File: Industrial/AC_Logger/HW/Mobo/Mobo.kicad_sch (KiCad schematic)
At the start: 6 parts

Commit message: Started new PCB
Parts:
- added A1: Arduino_UNO_R3, For_Rasterboard:Arduino_UNO_R3_WithMountingHoles_Snapped_to_P2.54mm, symbol MCU_Module:Arduino_UNO_R3
- added RTC2: Conn_01x05_Female, Connector_PinSocket_2.54mm:PinSocket_1x05_P2.54mm_Vertical, symbol Connector:Conn_01x05_Female
- added microSD2: Conn_01x06_Female, Connector_PinSocket_2.00mm:PinSocket_1x06_P2.00mm_Vertical, symbol Connector:Conn_01x06_Female
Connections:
- new net +3V3: A1.4 (3V3), RTC2.1 (Pin_1), microSD2.1 (Pin_1)
- new net GND: A1.29 (GND), RTC2.2 (Pin_2)
- new net SCL: A1.32 (SCL/A5), RTC2.3 (Pin_3)
- new net SDA: A1.31 (SDA/A4), RTC2.4 (Pin_4)

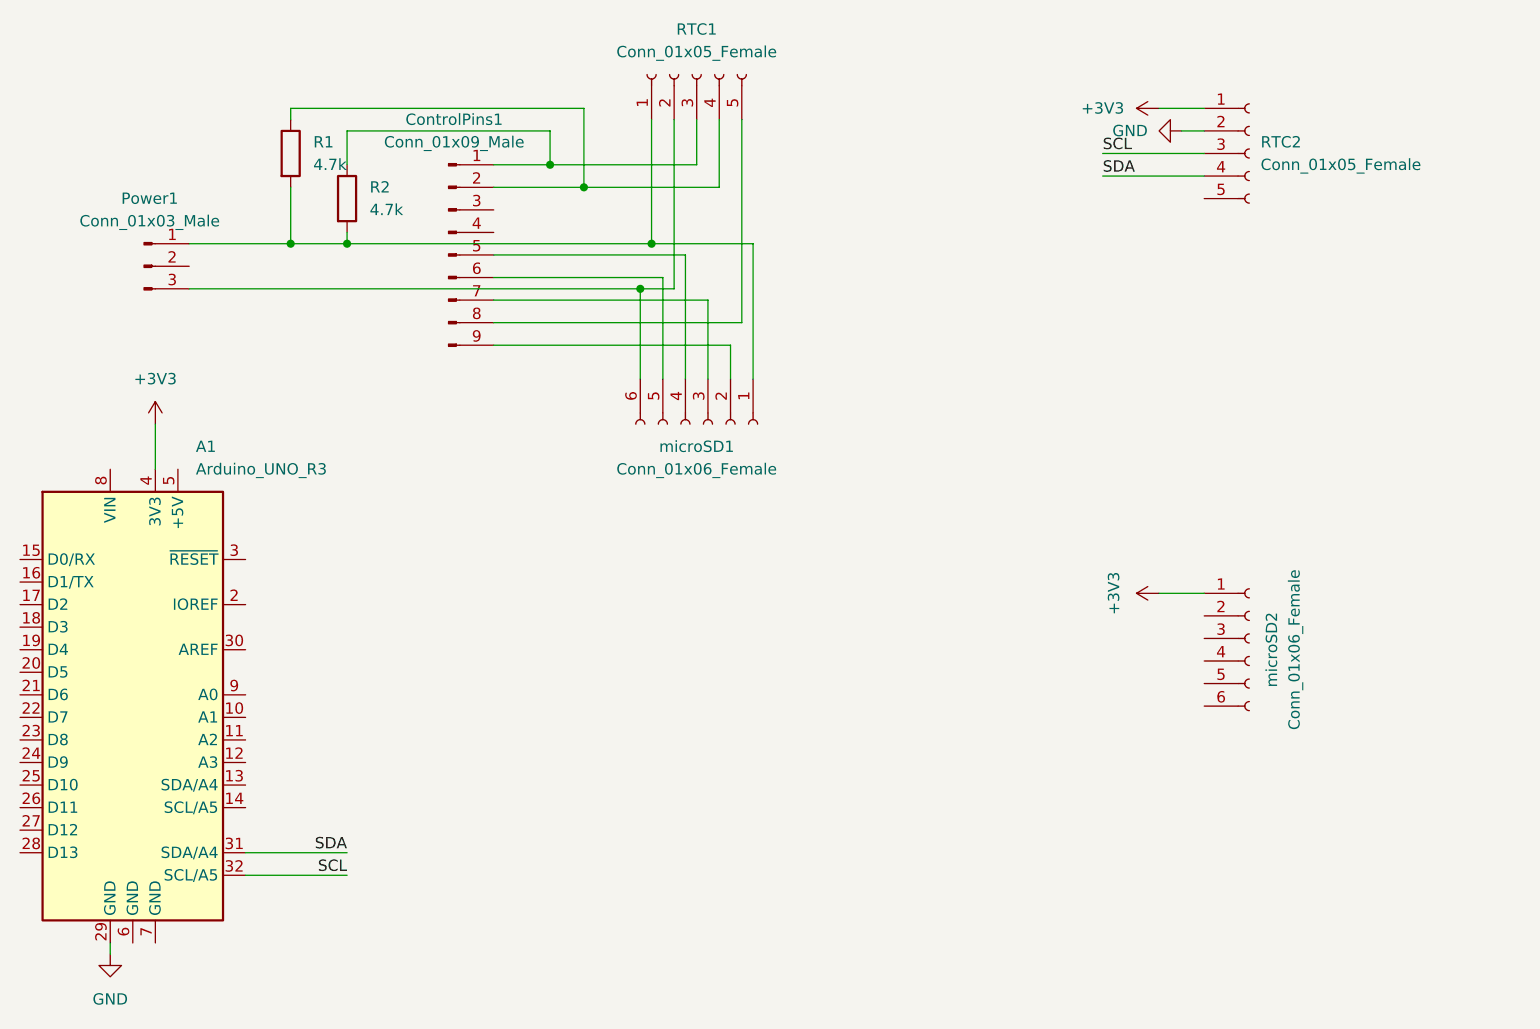
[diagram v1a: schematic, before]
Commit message: Finished stripboard design
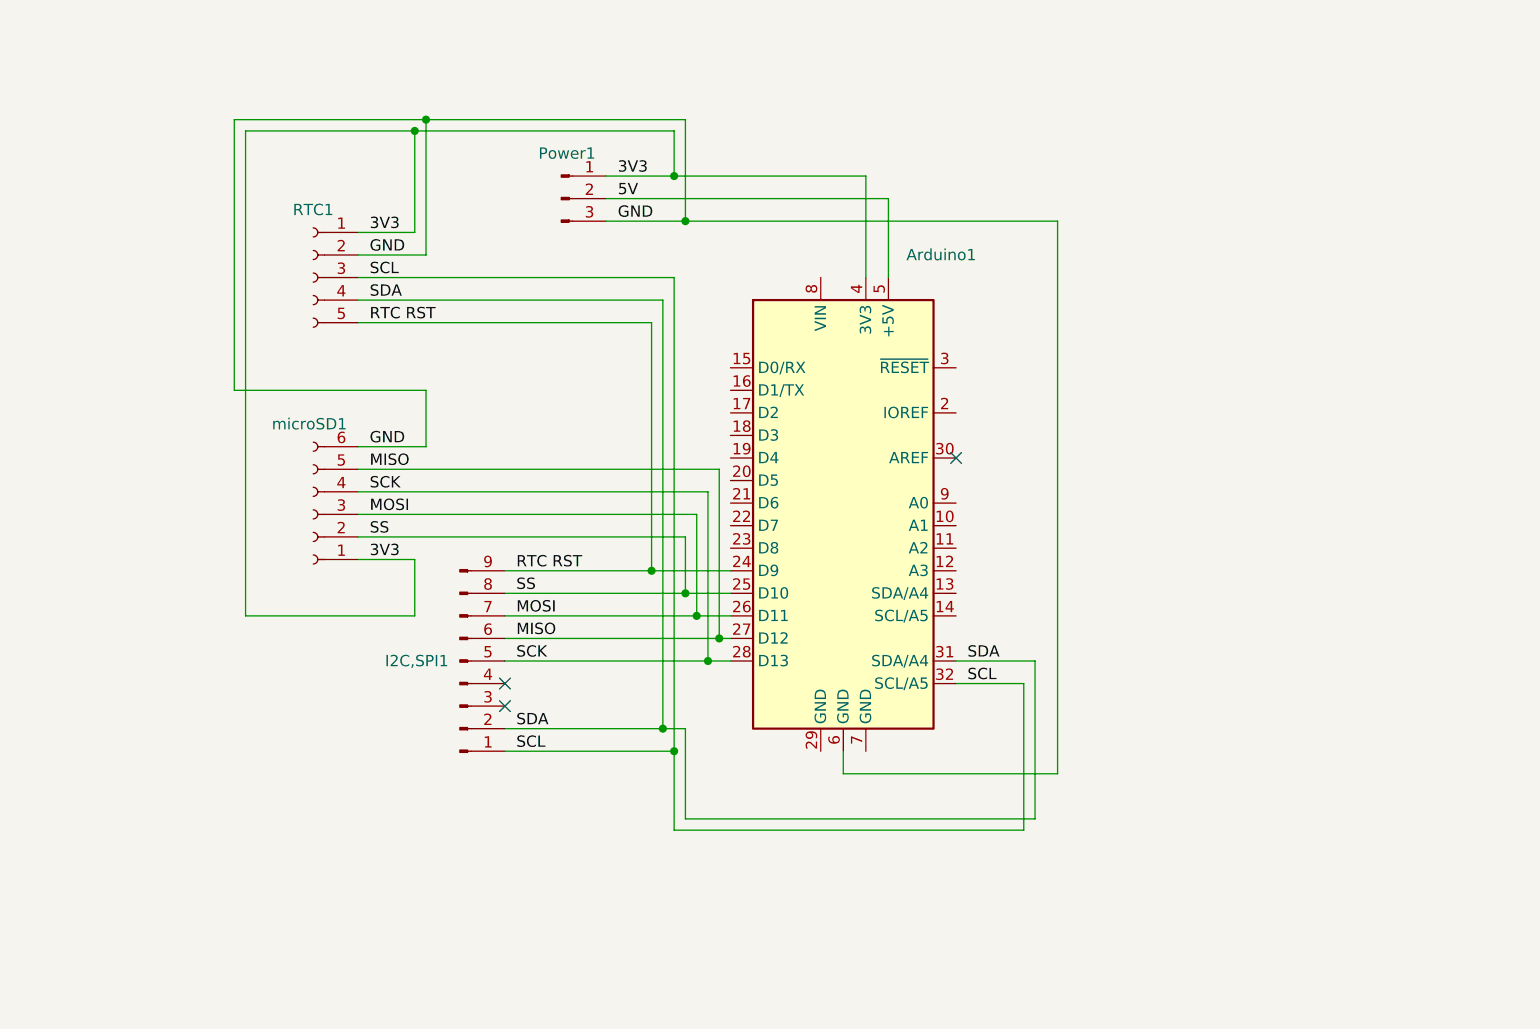
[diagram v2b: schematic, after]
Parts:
- removed R1, R2: 4.7k, Resistor_SMD:R_0402_1005Metric, symbol Device:R
- removed RTC1: Conn_01x05_Female, Connector_PinSocket_2.00mm:PinSocket_1x05_P2.00mm_Vertical, symbol Connector:Conn_01x05_Female
- removed microSD1: Conn_01x06_Female, Connector_PinSocket_2.00mm:PinSocket_1x06_P2.00mm_Vertical, symbol Connector:Conn_01x06_Female
- Arduino1: renamed from A1; value Arduino_UNO_R3 -> Arduino UNO R3
- I2C,SPI1: renamed from ControlPins1; footprint Connector_PinHeader_2.00mm:PinHeader_1x09_P2.00mm_Vertical -> Connector_PinHeader_2.54mm:PinHeader_1x09_P2.54mm_Vertical
- Power1: footprint Connector_PinHeader_2.00mm:PinHeader_1x03_P2.00mm_Vertical -> Connector_PinHeader_2.54mm:PinHeader_1x03_P2.54mm_Vertical
- microSD1: renamed from microSD2; footprint Connector_PinSocket_2.00mm:PinSocket_1x06_P2.00mm_Vertical -> Connector_PinSocket_2.54mm:PinSocket_1x06_P2.54mm_Vertical
- renumbered RTC2 to RTC1
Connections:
- net +3V3 is gone; now on net 3V3: Arduino1.4 (3V3), RTC1.1 (Pin_1), microSD1.1 (Pin_1)
- net GND: now also Arduino1.6 (GND), Power1.3 (Pin_3), microSD1.6 (Pin_6); no longer Arduino1.29 (GND)
- net SCL: now also I2C,SPI1.1 (Pin_1)
- net SDA: now also I2C,SPI1.2 (Pin_2)
- net 3V3: now reaches Power1.1 (Pin_1)
- net 5V: now reaches Power1.2 (Pin_2)
- net 5V: now also Arduino1.5 (+5V)
- net SS: now reaches microSD1.2 (Pin_2)
- net SS: now also Arduino1.25 (D10), I2C,SPI1.8 (Pin_8)
- net MOSI: now reaches microSD1.3 (Pin_3)
- net MOSI: now also Arduino1.26 (D11), I2C,SPI1.7 (Pin_7)
- net SCK: now reaches microSD1.4 (Pin_4)
- net SCK: now also Arduino1.28 (D13), I2C,SPI1.5 (Pin_5)
- net MISO: now reaches microSD1.5 (Pin_5)
- net MISO: now also Arduino1.27 (D12), I2C,SPI1.6 (Pin_6)
- net RTC RST: now reaches Arduino1.24 (D9)
- net RTC RST: now also I2C,SPI1.9 (Pin_9), RTC1.5 (Pin_5)
- no-connect marks 0 -> 3
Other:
- company: (none) -> Fakultet tehnickih nauka u Novom Sadu
- title: (none) -> Arduino Shield za DS1302 i MicroSD modul
- moved on the sheet: Arduino1, I2C,SPI1, Power1, RTC1, microSD1

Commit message: Last last edit to pcb
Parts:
- removed I2C,SPI1: Conn_01x09_Male, Connector_PinHeader_2.54mm:PinHeader_1x09_P2.54mm_Vertical, symbol Connector:Conn_01x09_Male
- removed Power1: Conn_01x03_Male, Connector_PinHeader_2.54mm:PinHeader_1x03_P2.54mm_Vertical, symbol Connector:Conn_01x03_Male
- added J1: Conn_01x11_Female, Connector_PinSocket_2.54mm:PinSocket_1x11_P2.54mm_Vertical, symbol Connector:Conn_01x11_Female
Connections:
- net 5V is gone; now on net +5V: Arduino1.5 (+5V)
- net GND: now also Arduino1.29 (GND), Arduino1.7 (GND), J1.2 (Pin_2), J1.3 (Pin_3)
- net RTC RST: now also Arduino1.23 (D8); no longer Arduino1.24 (D9)
- net A1: now reaches Arduino1.10 (A1)
- net A1: now also J1.7 (Pin_7)
- net A2: now reaches Arduino1.11 (A2)
- net A2: now also J1.8 (Pin_8)
- net A3: now reaches Arduino1.12 (A3)
- net A3: now also J1.9 (Pin_9)
- net A4: now reaches Arduino1.13 (SDA/A4)
- net A4: now also J1.10 (Pin_10)
- net A5: now reaches Arduino1.14 (SCL/A5)
- net A5: now also J1.11 (Pin_11)
- net VIN: now reaches Arduino1.8 (VIN)
- net VIN: now also J1.4 (Pin_4)
- net A0: now reaches Arduino1.9 (A0)
- net A0: now also J1.6 (Pin_6)
- net 3V3 renamed +5V
- net +5V: now also J1.1 (Pin_1); no longer Arduino1.4 (3V3)
- no-connect marks 3 -> 14
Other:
- moved on the sheet: RTC1, microSD1

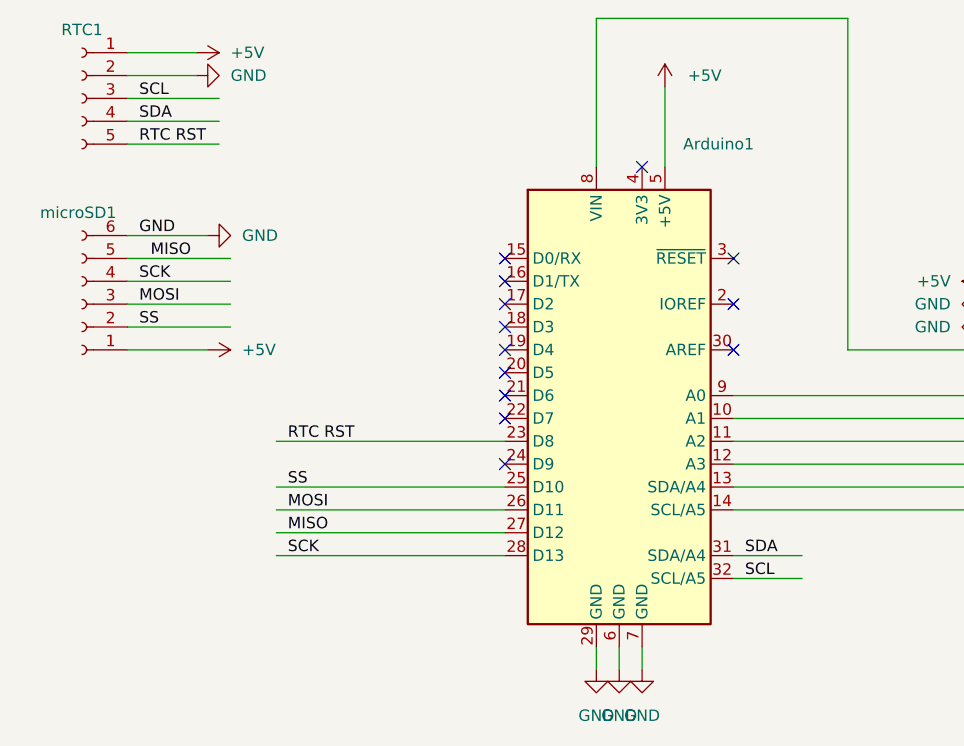
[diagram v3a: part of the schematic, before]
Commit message: PCB final, instructions for handling SD module
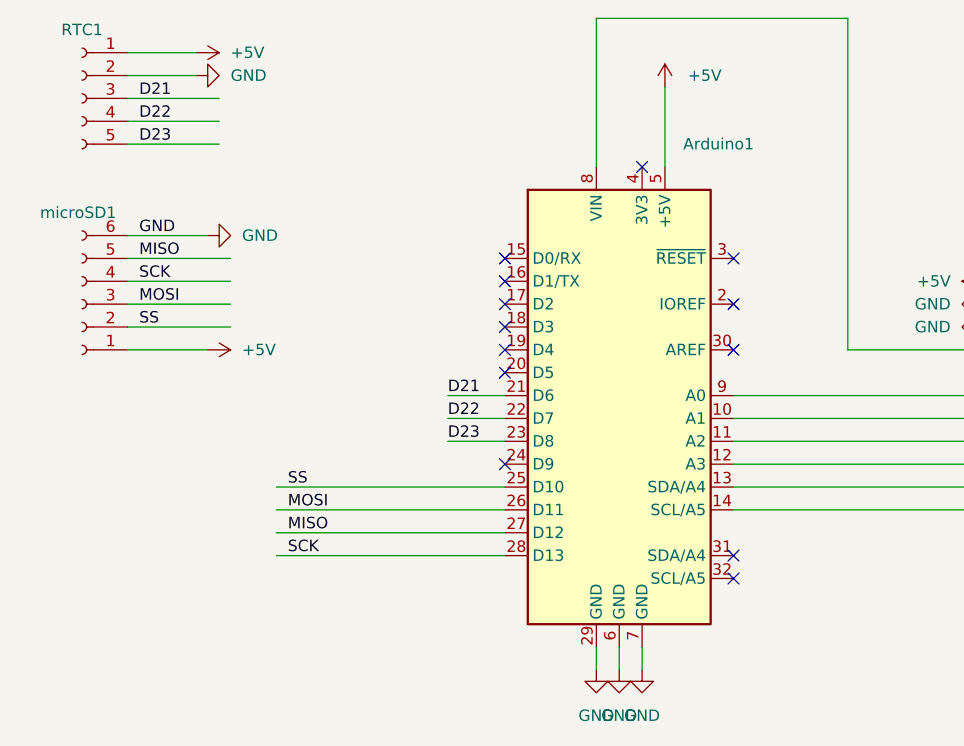
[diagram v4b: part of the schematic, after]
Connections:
- net D21: now reaches Arduino1.21 (D6)
- net D21: now also RTC1.3 (Pin_3)
- net D22: now reaches Arduino1.22 (D7)
- net D22: now also RTC1.4 (Pin_4)
- net RTC RST renamed D23
- net SCL: no longer names the net of Arduino1.32 (SCL/A5)
- net SCL: no longer RTC1.3 (Pin_3)
- net SDA: no longer names the net of Arduino1.31 (SDA/A4)
- net SDA: no longer RTC1.4 (Pin_4)
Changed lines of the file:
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@@
   (no_connect (at 148.59 83.82))
   (no_connect (at 148.59 86.36))
-  (no_connect (at 148.59 88.9))
   (no_connect (at 173.99 78.74))
   (no_connect (at 173.99 83.82))
-  (no_connect (at 148.59 91.44))
+  (no_connect (at 173.99 109.22))
   (no_connect (at 148.59 96.52))
   (no_connect (at 148.59 76.2))
   (no_connect (at 173.99 73.66))
+  (no_connect (at 173.99 106.68))
   (no_connect (at 148.59 81.28))
   (no_connect (at 163.83 63.5))
   (no_connect (at 148.59 73.66))
   (wire (pts (xy 106.68 73.66) (xy 118.11 73.66))
-    (stroke (width 0) (type default) (color 0 0 0 0))
-  )
-  (wire (pts (xy 181.61 109.22) (xy 173.99 109.22))
     (stroke (width 0) (type default) (color 0 0 0 0))
   )
@@
     (stroke (width 0) (type default) (color 0 0 0 0))
   )
-  (wire (pts (xy 173.99 106.68) (xy 181.61 106.68))
+  (wire (pts (xy 142.24 91.44) (xy 148.59 91.44))
     (stroke (width 0) (type default) (color 0 0 0 0))
   )
@@
     (stroke (width 0) (type default) (color 0 0 0 0))
   )
-  (wire (pts (xy 123.19 93.98) (xy 148.59 93.98))
-    (stroke (width 0) (type default) (color 0 0 0 0))
-  )
   (wire (pts (xy 158.75 46.99) (xy 158.75 63.5))
     (stroke (width 0) (type default) (color 0 0 0 0))
@@
     (stroke (width 0) (type default) (color 0 0 0 0))
   )
+  (wire (pts (xy 142.24 88.9) (xy 148.59 88.9))
+    (stroke (width 0) (type default) (color 0 0 0 0))
+  )
   (wire (pts (xy 106.68 55.88) (xy 116.84 55.88))
+    (stroke (width 0) (type default) (color 0 0 0 0))
+  )
+  (wire (pts (xy 142.24 93.98) (xy 148.59 93.98))
     (stroke (width 0) (type default) (color 0 0 0 0))
   )
@@
     (stroke (width 0) (type default) (color 0 0 0 0))
   )
-  (label "RTC RST" (at 107.95 60.96 0)
+  (label "D23" (at 107.95 60.96 0)
+    (effects (font (size 1.27 1.27)) (justify left bottom))
+  )
+  (label "D23" (at 142.24 93.98 0)
     (effects (font (size 1.27 1.27)) (justify left bottom))
   )
@@
     (effects (font (size 1.27 1.27)) (justify left bottom))
   )
-  (label "MISO" (at 109.22 73.66 0)
+  (label "MISO" (at 107.95 73.66 0)
     (effects (font (size 1.27 1.27)) (justify left bottom))
   )
-  (label "SDA" (at 107.95 58.42 0)
+  (label "D22" (at 107.95 58.42 0)
+    (effects (font (size 1.27 1.27)) (justify left bottom))
+  )
+  (label "D22" (at 142.24 91.44 0)
     (effects (font (size 1.27 1.27)) (justify left bottom))
   )
@@
   )
   (label "A3" (at 205.74 96.52 0)
-    (effects (font (size 1.27 1.27)) (justify left bottom))
-  )
-  (label "RTC RST" (at 124.46 93.98 0)
     (effects (font (size 1.27 1.27)) (justify left bottom))
   )
@@
   )
   (label "MOSI" (at 107.95 78.74 0)
-    (effects (font (size 1.27 1.27)) (justify left bottom))
-  )
-  (label "SDA" (at 175.26 106.68 0)
     (effects (font (size 1.27 1.27)) (justify left bottom))
   )
@@
     (effects (font (size 1.27 1.27)) (justify left bottom))
   )
-  (label "SCL" (at 175.26 109.22 0)
-    (effects (font (size 1.27 1.27)) (justify left bottom))
-  )
   (label "MOSI" (at 124.46 101.6 0)
     (effects (font (size 1.27 1.27)) (justify left bottom))
   )
-  (label "SCL" (at 107.95 55.88 0)
+  (label "D21" (at 107.95 55.88 0)
     (effects (font (size 1.27 1.27)) (justify left bottom))
   )
@@
     (effects (font (size 1.27 1.27)) (justify left bottom))
   )
+  (label "D21" (at 142.24 88.9 0)
+    (effects (font (size 1.27 1.27)) (justify left bottom))
+  )

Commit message: Finising touches on PCB and Schematic
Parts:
- added R1, R2: 4K7, Resistor_THT:R_Axial_DIN0207_L6.3mm_D2.5mm_P7.62mm_Horizontal, symbol Device:R
- renumbered J1 to V_Sensors_Header1
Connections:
- net +5V: now also R1.2, R2.2
- net D21: now also R1.1
- net D22: now also R2.1
- net GND: no longer Arduino1.29 (GND), Arduino1.7 (GND), RTC1.2 (Pin_2), microSD1.6 (Pin_6)
- net A0: no longer names the net of Arduino1.9 (A0), V_Sensors_Header1.6 (Pin_6)
- net A1: no longer names the net of Arduino1.10 (A1), V_Sensors_Header1.7 (Pin_7)
- net A2: no longer names the net of Arduino1.11 (A2), V_Sensors_Header1.8 (Pin_8)
- net A3: no longer names the net of Arduino1.12 (A3), V_Sensors_Header1.9 (Pin_9)
- net A4: no longer names the net of Arduino1.13 (SDA/A4), V_Sensors_Header1.10 (Pin_10)
- net A5: no longer names the net of Arduino1.14 (SCL/A5), V_Sensors_Header1.11 (Pin_11)
- new net GND1: Arduino1.29 (GND), RTC1.2 (Pin_2), microSD1.6 (Pin_6)
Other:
- moved on the sheet: RTC1, V_Sensors_Header1, microSD1
